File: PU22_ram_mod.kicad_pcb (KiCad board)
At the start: 2 copper layers, 104.6 x 39.1 mm, 12 parts, among them J1 MOBO, J2 BA8, J3 BA10, J4 GND

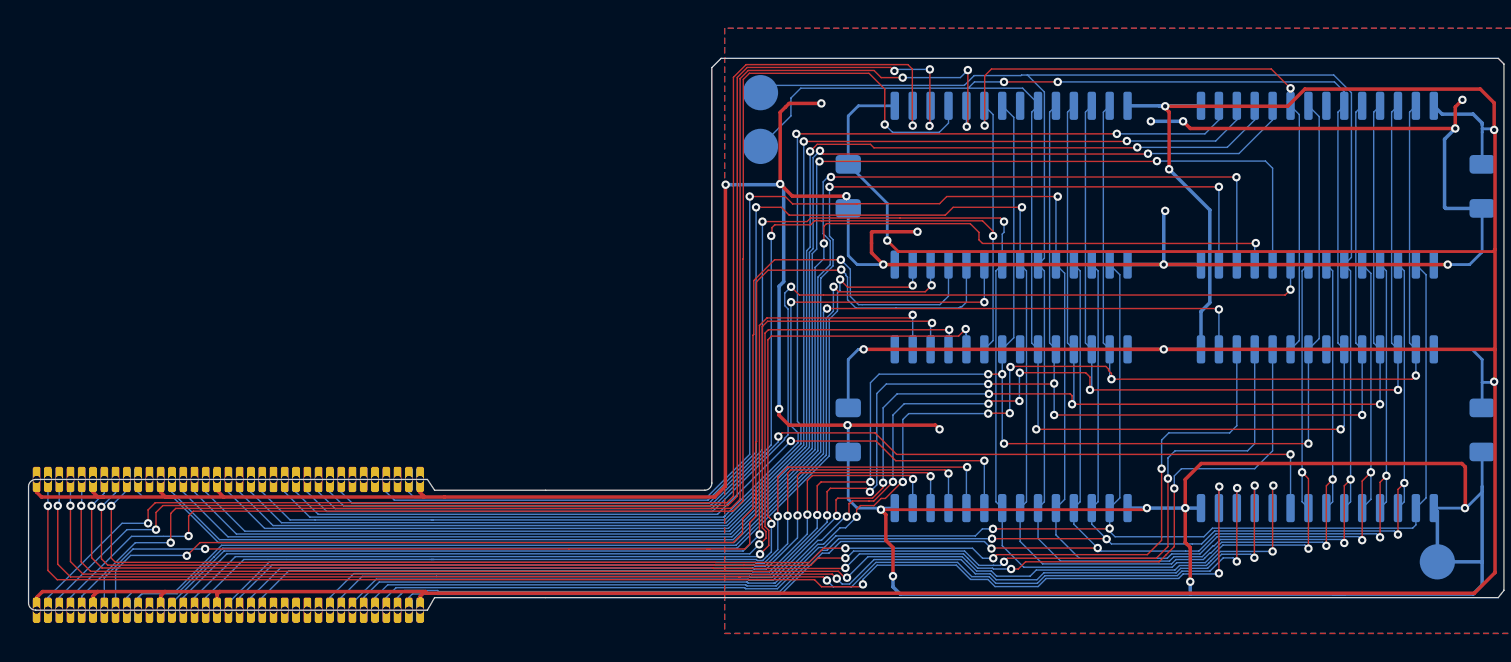
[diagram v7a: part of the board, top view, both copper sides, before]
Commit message: Update the routing of some traces to increase distance from pads
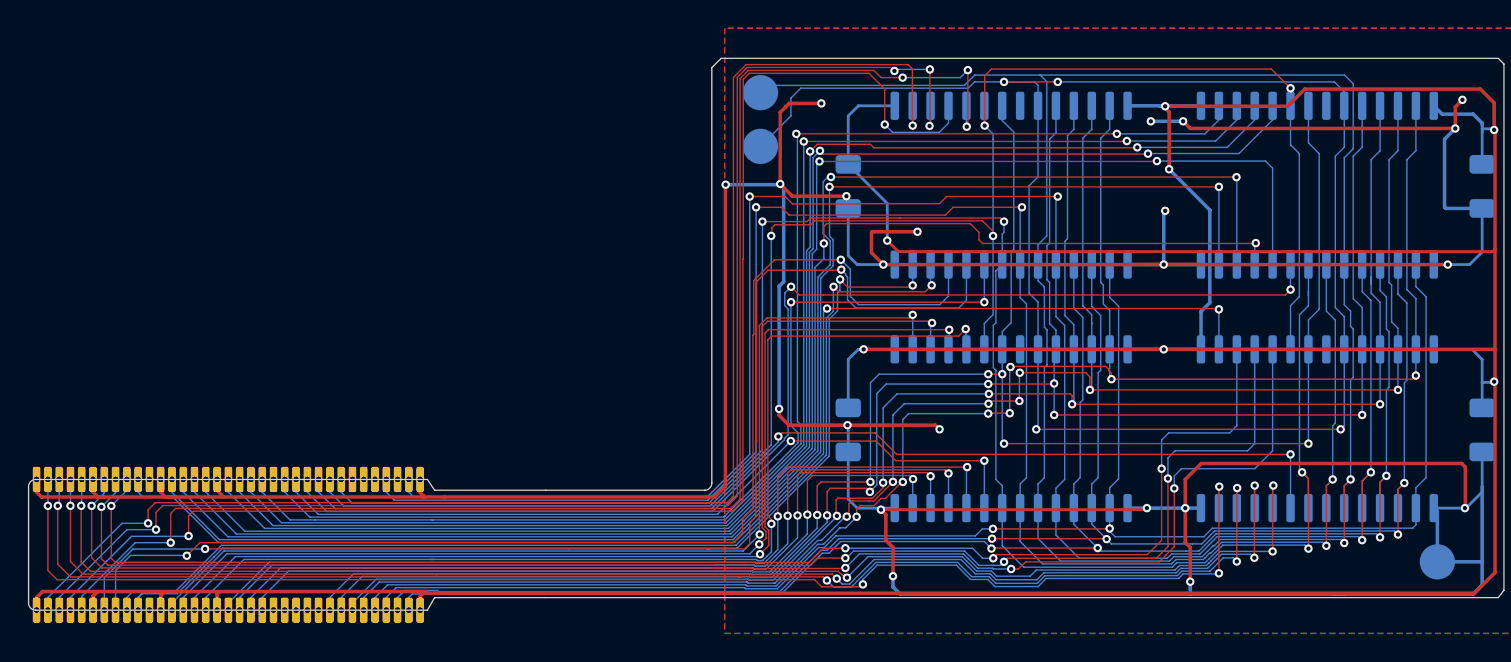
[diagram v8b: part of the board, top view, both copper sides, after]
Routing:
- net /~{WE}: track 130.6 -> 129.1 mm
- net /A10: track 119.3 -> 118.0 mm
- net /A1: track 127.5 -> 128.3 mm
- net /A8: track 134.8 -> 135.4 mm
- net /~{OE}: track 135.9 -> 136.6 mm
